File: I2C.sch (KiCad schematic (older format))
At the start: 2 parts, among them U1 PCA9306

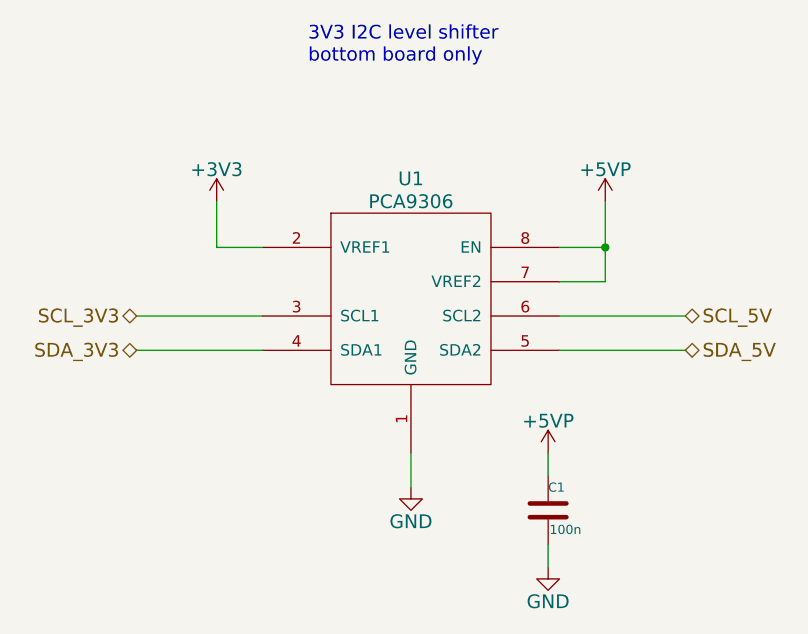
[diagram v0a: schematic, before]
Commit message: Renamed solenoid to v1.1, added part descriptions
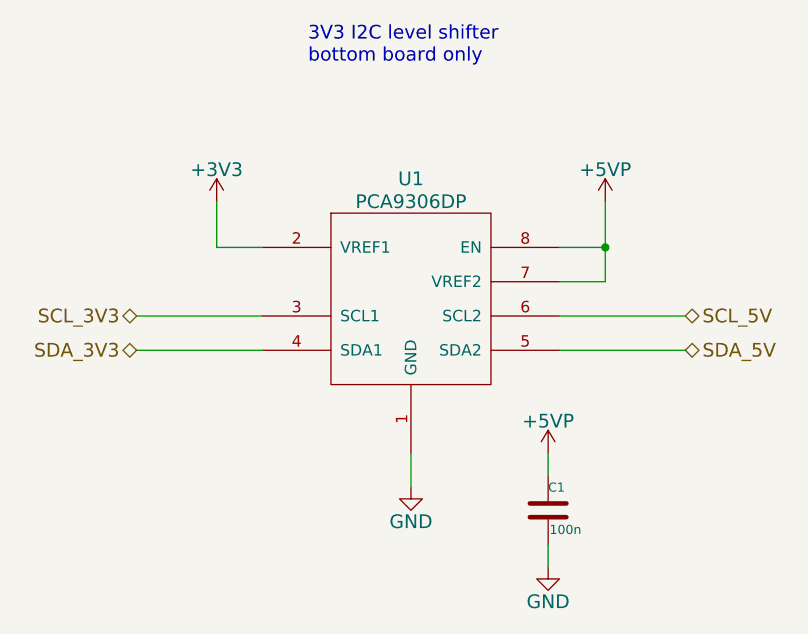
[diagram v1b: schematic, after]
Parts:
- C1: Alt. Order Code (none) -> 710-885012207098; Alt. Supplier (none) -> Mouser; Note (none) -> 100nF/50V X7R 0805 ceramic capacitor; Package (none) -> 0805; Supplier (none) -> Farnell
- U1: value PCA9306 -> PCA9306DP; Alt. Order Code (none) -> 771-PCA9306DP-T; Alt. Supplier (none) -> Mouser; Manufacturer NXP -> NXP Semiconductors; Note (none) -> Dual I²C-bus voltage translator; Package (none) -> TSSOP-8; Supplier (none) -> Farnell
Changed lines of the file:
@@
 EESchema Schematic File Version 2
-LIBS:MicroFLiC_servo_solenoid_1_0-rescue
 LIBS:power
 LIBS:device
@@
 LIBS:valves
 LIBS:jakub
-LIBS:MicroFLiC_servo_solenoid_1_0-cache
+LIBS:MicroFLiC_servo_solenoid-cache
 EELAYER 25 0
 EELAYER END
@@
 P 4850 2700
 F 0 "U1" H 4850 3200 60  0000 C CNN
-F 1 "PCA9306" H 4850 3100 60  0000 C CNN
+F 1 "PCA9306DP" H 4850 3100 60  0000 C CNN
 F 2 "Housings_SSOP:TSSOP-8_3x3mm_Pitch0.65mm" H 4850 2700 60  0001 C CNN
 F 3 "" H 4850 2700 60  0000 C CNN
 F 4 "PCA9306DP" H 4850 2700 60  0001 C CNN "Part Number"
-F 5 "NXP" H 4850 2700 60  0001 C CNN "Manufacturer"
-F 6 "2212072" H 4850 2700 60  0001 C CNN "Order Code"
+F 5 "NXP Semiconductors" H 4850 2700 60  0001 C CNN "Manufacturer"
+F 6 "TSSOP-8" H 4850 2700 60  0001 C CNN "Package"
+F 7 "Farnell" H 4850 2700 60  0001 C CNN "Supplier"
+F 8 "2212072" H 4850 2700 60  0001 C CNN "Order Code"
+F 9 "Mouser" H 4850 2700 60  0001 C CNN "Alt. Supplier"
+F 10 "771-PCA9306DP-T" H 4850 2700 60  0001 C CNN "Alt. Order Code"
+F 11 "Dual I²C-bus voltage translator" H 4850 2700 60  0001 C CNN "Note"
 	1    4850 2700
 	1    0    0    -1
@@
 U 1 1 54D96092
 P 5450 3650
-AR Path="/54D96092" Ref="C1"  Part="1"
-AR Path="/54D957C7/54D96092" Ref="C1"  Part="1"
 F 0 "C1" H 5450 3750 40  0000 L CNN
 F 1 "100n" H 5456 3565 40  0000 L CNN
@@
 F 4 "MC0805B104K250CT" H 5450 3650 60  0001 C CNN "Part Number"
 F 5 "Multicomp" H 5450 3650 60  0001 C CNN "Manufacturer"
-F 6 "1759166" H 5450 3650 60  0001 C CNN "Order Code"
+F 6 "0805" H 5450 3650 60  0001 C CNN "Package"
+F 7 "Farnell" H 5450 3650 60  0001 C CNN "Supplier"
+F 8 "1759166" H 5450 3650 60  0001 C CNN "Order Code"
+F 9 "Mouser" H 5450 3650 60  0001 C CNN "Alt. Supplier"
+F 10 "710-885012207098" H 5450 3650 60  0001 C CNN "Alt. Order Code"
+F 11 "100nF/50V X7R 0805 ceramic capacitor" H 5450 3650 60  0001 C CNN "Note"
 	1    5450 3650
 	1    0    0    -1
